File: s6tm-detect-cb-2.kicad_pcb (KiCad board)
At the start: 4 copper layers, 90 x 50 mm, 173 parts, among them J1 Conn_Coaxial, J2 Conn_01x04_Pin, J3 USB_C_Receptacle_USB2.0_14P, J4 Conn_01x04, J5 Conn_01x04, J6 USB_C_Receptacle_USB2.0_14P, J7 Conn_01x04_Pin, J8 SIM_Card_Shielded, J9 Conn_Coaxial, Q1 AO3400A, Q2 MMBT3904, Q3 MMBT3904, Q4 MMBT3904, SW1 SW_Push, SW2 SW_Push, SW3 SW_Push, SW4 SW_Push, U1 W25Q128JVS, U10 TPS6282x, U11 TPS6282x, U12 TPS259472A, U13 TPD3F303DPV, U14 SIM7080G, U15 SN74LV1T125DBV, U16 SN74LV1T125DBV, U17 SN74LV1T125DBV, U18 SN74LV1T125DBV, U19 SN74LV1T125DBV, U2 SN65HVD230, U3 PCF85263ATL, U4 MS5607, U5 ESP32-S3FH4R2, U6 HTU21, U8 VL53L0CXV0DH1, U9 NextPM, Y1 32k768, Y2 48M

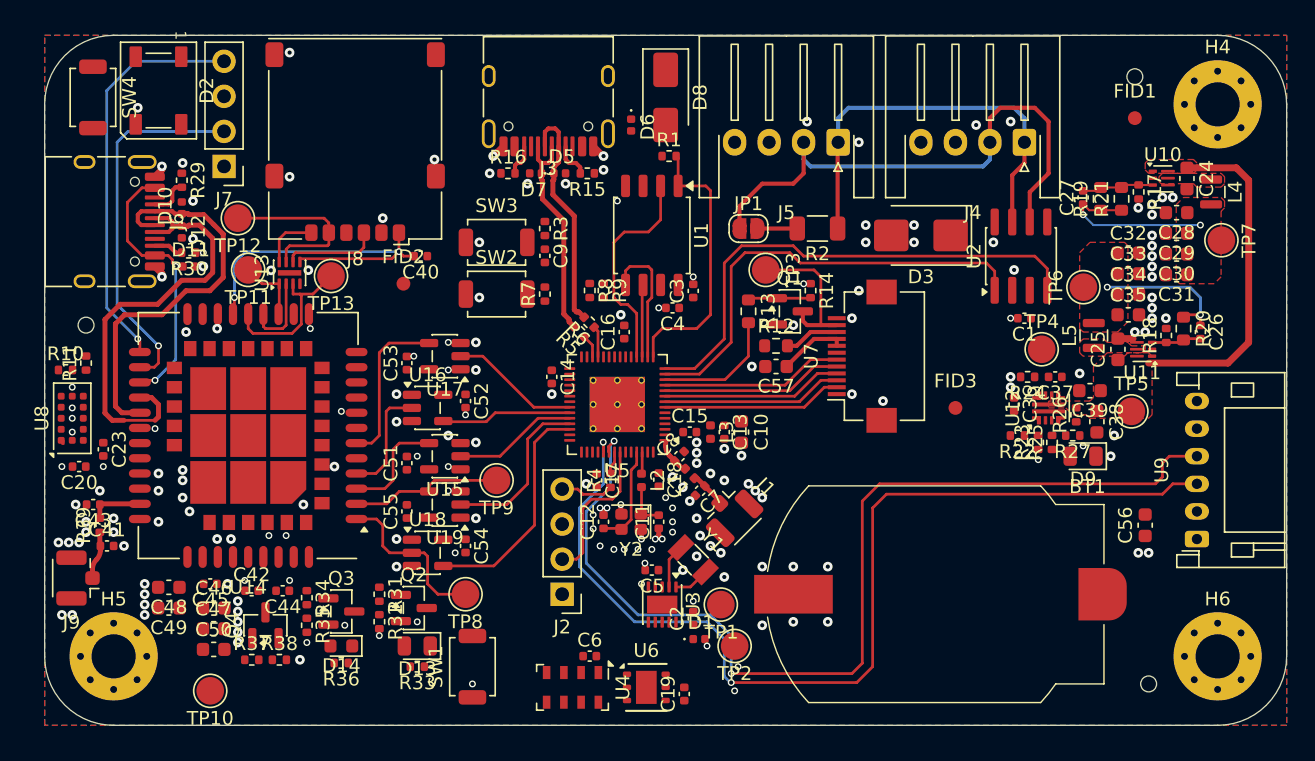
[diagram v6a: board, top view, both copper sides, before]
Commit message: pcb: route i2c
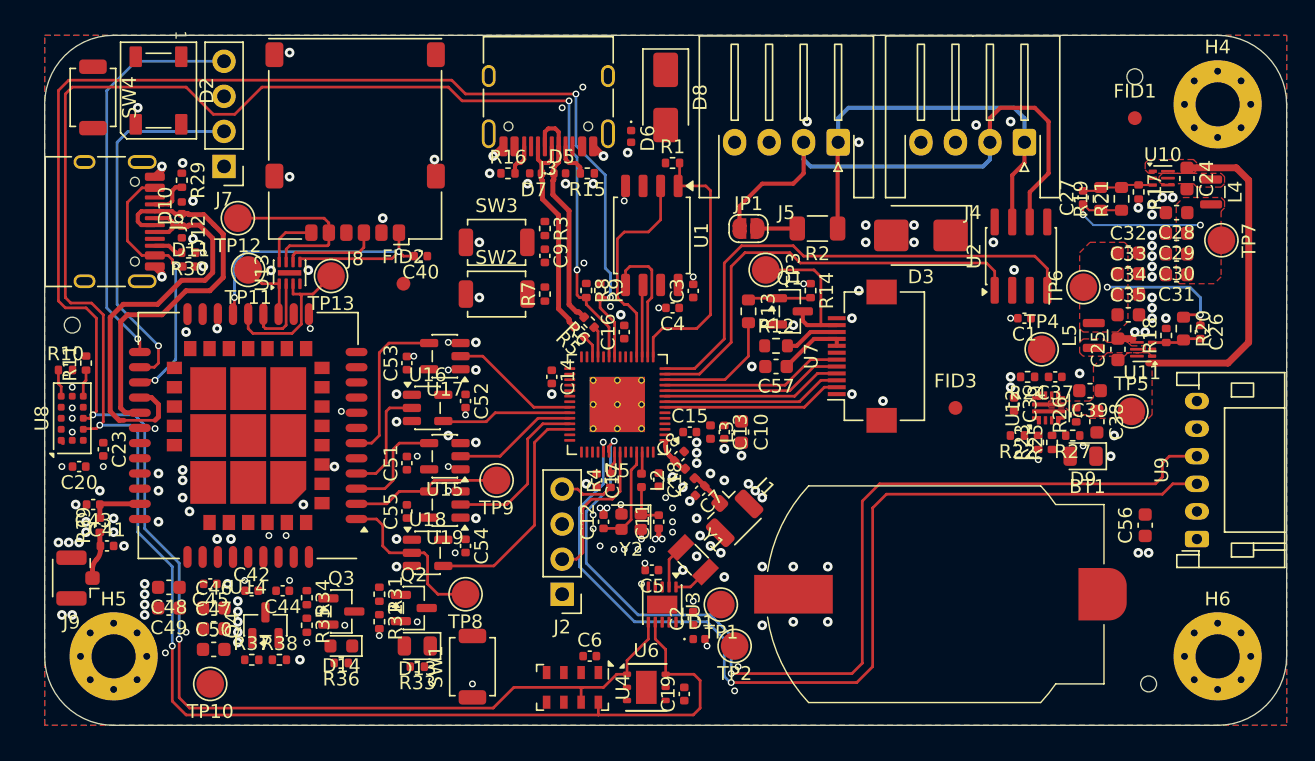
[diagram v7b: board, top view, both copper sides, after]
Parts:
- moved H2 1.00 mm to (101.0, 88.0)
- moved D6 0.83 mm to (141.5, 74.3)
- moved R1 0.56 mm to (144.5, 76.2)
- moved TP10 0.50 mm to (111.0, 114.0)
- moved R8 0.25 mm to (138.2, 85.5)
- moved R9 0.25 mm to (139.2, 85.5)
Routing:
- net /SCL: track 0.00 -> 158.3 mm, vias 0 -> 4
- net /SDA: track 0.00 -> 150.2 mm, vias 0 -> 4
- net Net-(U8-XSHUT): track 0.00 -> 1.98 mm
- net /TOF_INT: track 0.00 -> 1.97 mm
- net /Cellular/MODEM_D+: track 31.8 -> 31.1 mm
- net /Cellular/MODEM_D-: track 29.1 -> 28.5 mm
- net /FLASH_CS: track 19.9 -> 19.4 mm
- net GND: vias 191 -> 198
